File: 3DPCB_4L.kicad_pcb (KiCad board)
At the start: 4 copper layers, 100 x 60 mm, 740 parts, among them IC1 A5984_LP, IC2 A5984_LP, IC3 A5984_LP, IC4 A5984_LP, IC5 A5984_LP, IC6 MP9943, J10 , J11 , J12 , J13 , J14 , J15 , J16 , J2 , J3 , J4 , J5 , J6 , J7 , J8 , J9 , K1 CONN_3, K2 CONN_3, K3 CONN_3, K4 CONN_3, K5 CONN_3, K6 CONN_3, K7 CONN_3, K8 CONN_3, K9 CONN_3, P1 CONN_8, P11 CONN_3X2, P12 CONN_3X2, P13 CONN_4, P2 CONN_8, P5 CONN_4, P6 CONN_4, P7 CONN_4, P8 CONN_02X03, P9 CONN_4, U1 CONN_4_LERCHE, U10 MICRO-SD, U11 TC4427, U12 MCP4728, U13 CONN_4_LERCHE, U15 SPST_MOMENTARY, U16 CONN_4_LERCHE, U2 SPST_MOMENTARY, U21 CONN_4_LERCHE, U22 CONN_4_LERCHE, U23 MCP4728, U24 IRFH5302, U25 CONN_4_LERCHE, U3 BSS84, U4 CONN_4_LERCHE, U5 IRFH5302, U6 LPC1768_TQFP100, U7 IRFH5302, U8 IRFH5302, U9 TC4427

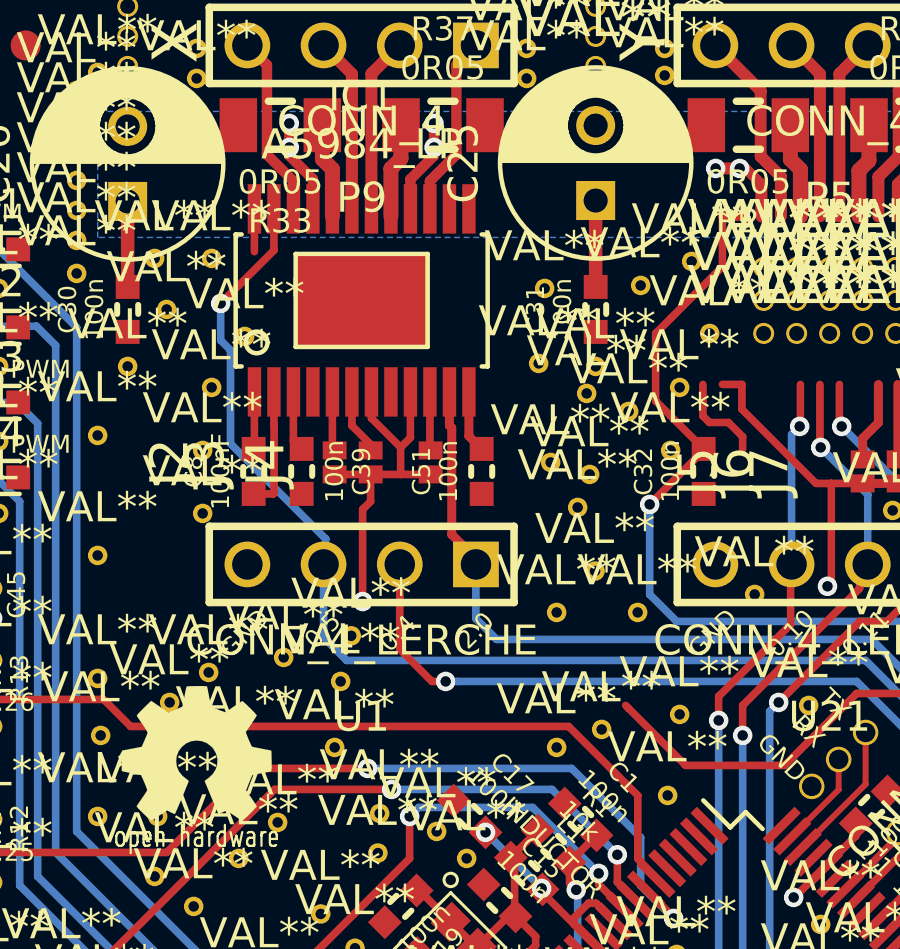
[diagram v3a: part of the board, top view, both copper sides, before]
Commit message: DONT USE NOW
Still working on PCB.
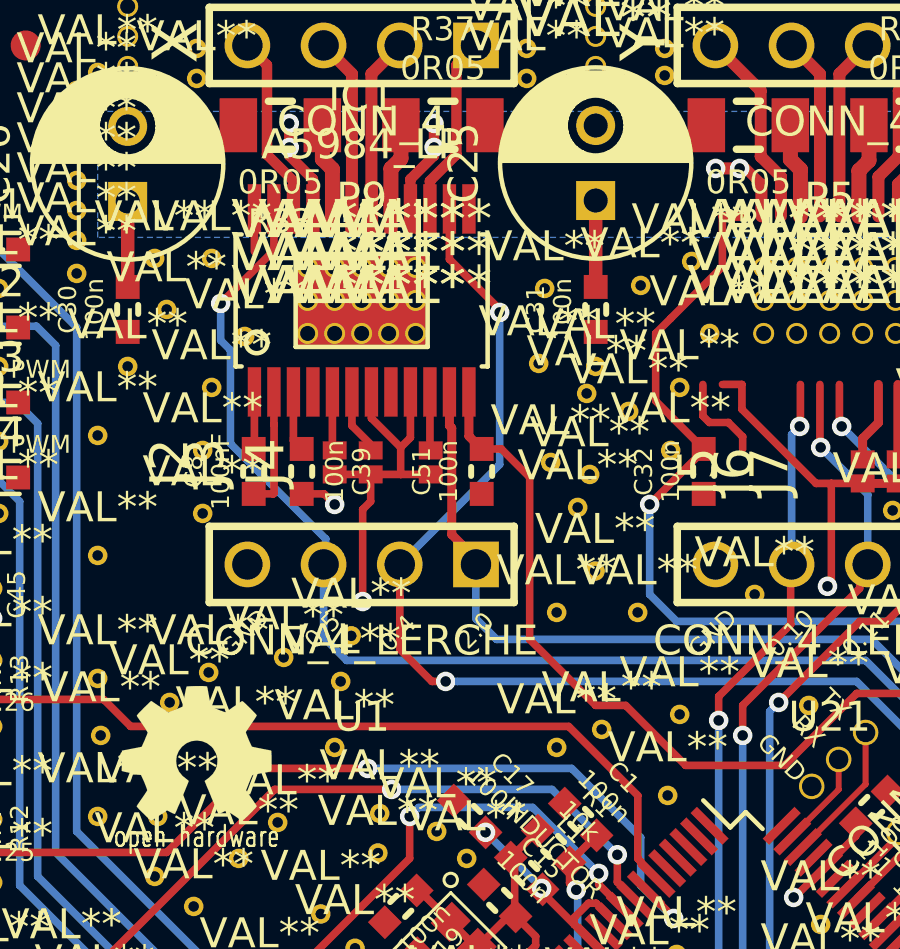
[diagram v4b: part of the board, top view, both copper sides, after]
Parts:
- added ?: VAL**, Lerche_via_0.5mm_GND, F.Cu at (150.6, 147.4)
- added ?: VAL**, Lerche_via_0.5mm_GND, F.Cu at (151.5, 145.2)
- added ?: VAL**, Lerche_via_0.5mm_GND, F.Cu at (149.7, 145.2)
- added ?: VAL**, Lerche_via_0.5mm_GND, F.Cu at (147.9, 145.2)
- added ?: VAL**, Lerche_via_0.5mm_GND, F.Cu at (147.9, 146.3)
- added ?: VAL**, Lerche_via_0.5mm_GND, F.Cu at (151.5, 146.3)
- added ?: VAL**, Lerche_via_0.5mm_GND, F.Cu at (149.7, 146.3)
- added ?: VAL**, Lerche_via_0.5mm_GND, F.Cu at (150.6, 146.3)
- added ?: VAL**, Lerche_via_0.5mm_GND, F.Cu at (150.6, 145.2)
- added ?: VAL**, Lerche_via_0.5mm_GND, F.Cu at (148.8, 145.2)
- added ?: VAL**, Lerche_via_0.5mm_GND, F.Cu at (148.8, 146.3)
- added ?: VAL**, Lerche_via_0.5mm_GND, F.Cu at (148.8, 147.4)
- added ?: VAL**, Lerche_via_0.5mm_GND, F.Cu at (147.9, 147.4)
- added ?: VAL**, Lerche_via_0.5mm_GND, F.Cu at (149.7, 147.4)
- added ?: VAL**, Lerche_via_0.5mm_GND, F.Cu at (151.5, 147.4)
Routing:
- net DIR1: track 33.0 -> 46.9 mm, vias 2 -> 3
- net VREF1: track 31.9 -> 43.4 mm
- net +12V: track 55.1 -> 56.3 mm, vias 9 -> 10

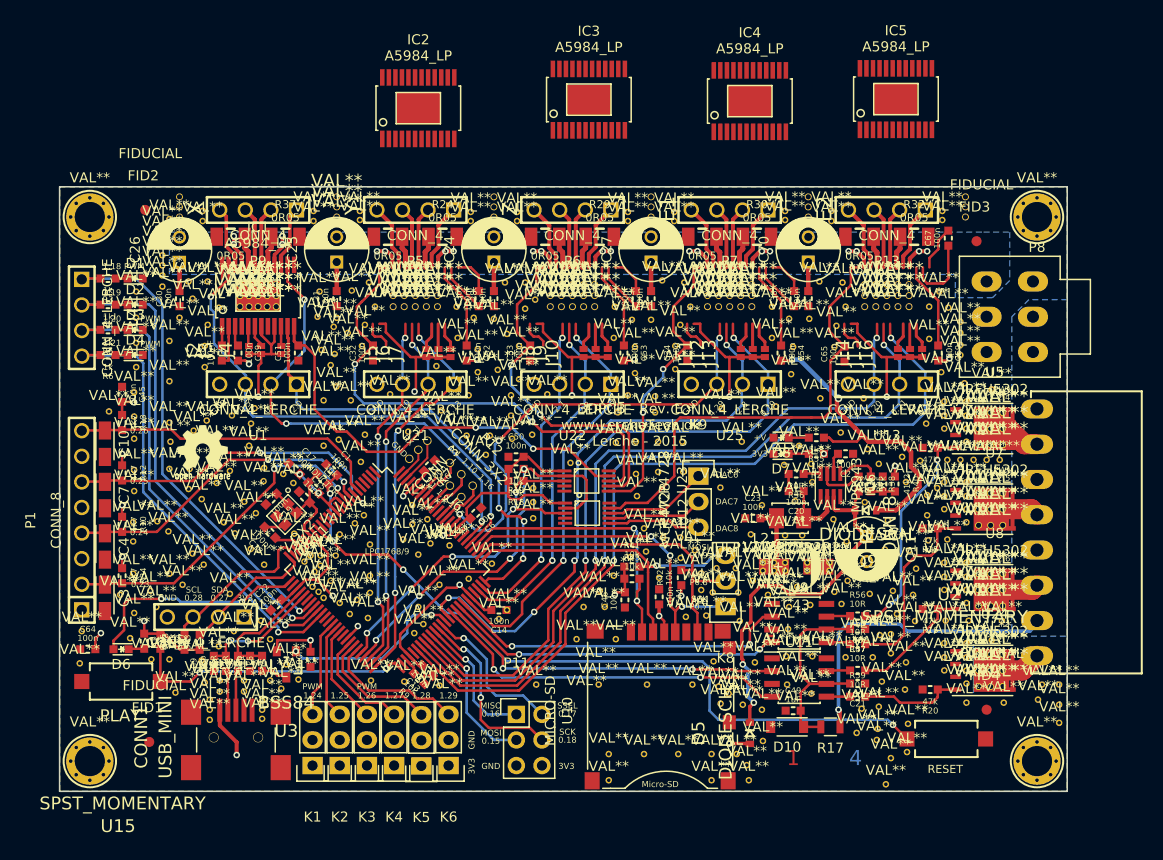
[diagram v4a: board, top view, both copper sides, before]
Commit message: Wired all connections with A5984 on PCB
UNTESTED - Do not use now.
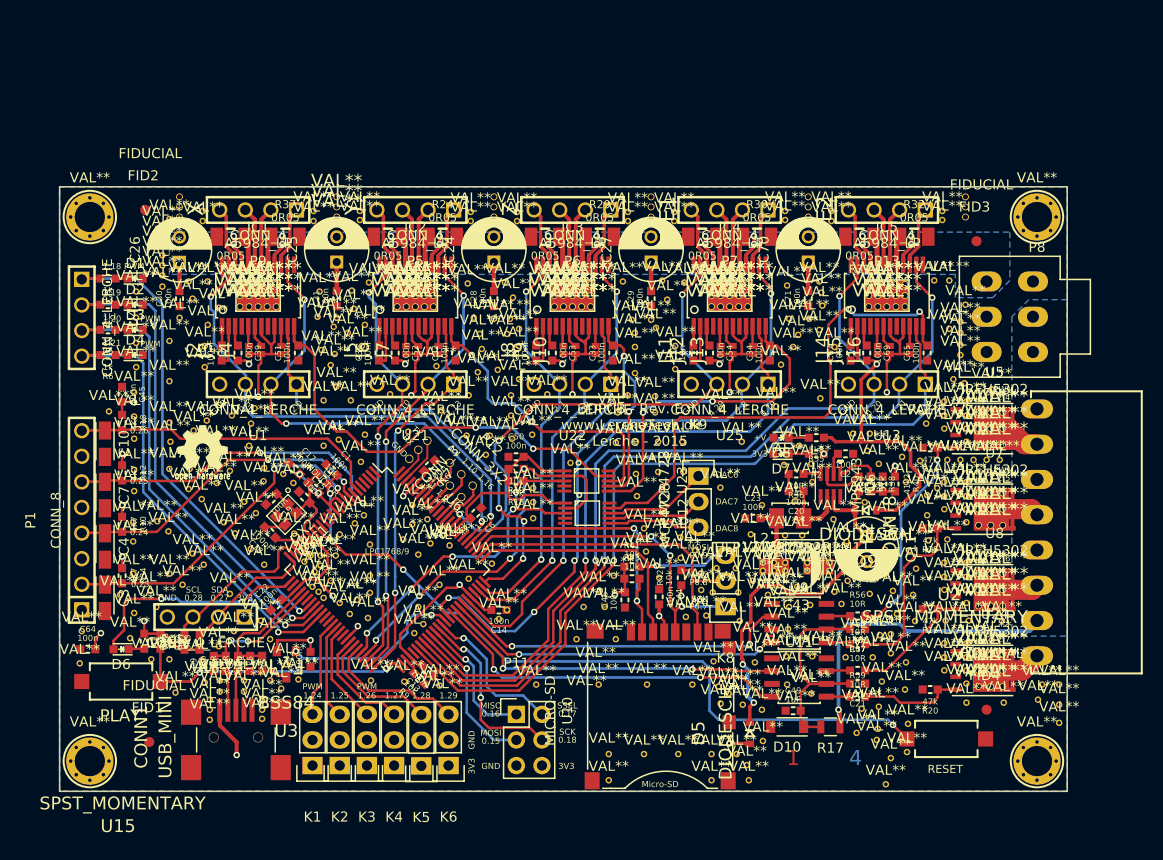
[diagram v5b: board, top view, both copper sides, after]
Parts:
- moved IC5 19.5 mm to (212.1, 146.3)
- moved IC3 19.5 mm to (180.9, 146.3)
- moved IC4 19.4 mm to (196.5, 146.3)
- moved IC2 18.6 mm to (165.3, 146.3)
- moved C67 15.0 mm to (208.5, 152.0)
- moved C38 11.4 mm to (192.9, 152.0)
- moved C36 11.3 mm to (161.7, 152.0)
- moved C37 11.3 mm to (177.3, 152.0)
- moved ? 9.14 mm to (218.3, 144.8)
- moved C65 8.20 mm to (216.1, 152.0)
- moved C32 8.20 mm to (169.3, 152.0)
- moved C33 8.20 mm to (184.9, 152.0)
- moved C34 8.20 mm to (200.5, 152.0)
- moved ? 7.59 mm to (218.7, 154.6)
- moved C52 7.10 mm to (163.3, 152.0)
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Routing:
- net (no net): track 35.6 -> 0.68 mm, vias 16 -> 0
- net +12V: track 56.3 -> 78.6 mm, vias 10 -> 25
- net VREF2: track 49.8 -> 29.9 mm
- net VREF3: track 35.1 -> 19.3 mm
- net EN5: track 73.4 -> 81.2 mm
- net EN4: track 45.4 -> 53.3 mm
- net EN3: track 32.5 -> 40.4 mm
- net EN2: track 35.4 -> 43.2 mm
- net DIR2: track 38.0 -> 45.4 mm
- net DIR5: track 77.0 -> 84.2 mm
- net DIR3: track 35.0 -> 42.1 mm
- net DIR4: track 57.8 -> 64.7 mm
- net Net-(C53-Pad2): track 8.65 -> 2.01 mm
- net Net-(C52-Pad2): track 8.65 -> 2.01 mm
- net Net-(C69-Pad2): track 8.65 -> 2.01 mm
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
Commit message: Moved vias around
Moved vias around
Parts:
- added ?: VAL**, Lerche_via_0.35mm_GND_MaskOver, F.Cu at (228.7, 145.4)
- added ?: VAL**, Lerche_via_0.35mm_GND_MaskOver, F.Cu at (220.6, 150.2)
- added ?: VAL**, Lerche_via_0.35mm_GND_MaskOver, F.Cu at (189.6, 166.7)
- added ?: VAL**, Lerche_via_0.35mm_GND_MaskOver, F.Cu at (191.3, 167.4)
- added ?: VAL**, Lerche_via_0.35mm_GND_MaskOver, F.Cu at (201.1, 164.8)
- added ?: VAL**, Lerche_via_0.35mm_GND_MaskOver, F.Cu at (198.8, 157.6)
- added ?: VAL**, Lerche_via_0.35mm_GND_MaskOver, F.Cu at (193.9, 157.7)
- added ?: VAL**, Lerche_via_0.35mm_GND_MaskOver, F.Cu at (197.7, 159.1)
- added ?: VAL**, Lerche_via_0.35mm_GND_MaskOver, F.Cu at (203.3, 155.1)
- added ?: VAL**, Lerche_via_0.35mm_GND_MaskOver, F.Cu at (207.3, 156.8)
- added ?: VAL**, Lerche_via_0.35mm_GND_MaskOver, F.Cu at (201.3, 144.9)
- added ?: VAL**, Lerche_via_0.35mm_GND_MaskOver, F.Cu at (228.6, 143.0)
- added ?: VAL**, Lerche_via_0.35mm_GND_MaskOver, F.Cu at (201.6, 147.9)
- added ?: VAL**, Lerche_via_0.35mm_GND_MaskOver, F.Cu at (184.5, 147.7)
- added ?: VAL**, Lerche_via_0.35_GND_MaskOver, F.Cu at (173.0, 148.5)
- added ?: VAL**, Lerche_via_0.35mm_GND_MaskOver, F.Cu at (226.9, 143.0)
- added ?: VAL**, Lerche_via_0.35mm_GND_MaskOver, F.Cu at (225.3, 143.0)
- added ?: VAL**, Lerche_via_0.35mm_GND_MaskOver, F.Cu at (224.9, 145.9)
- added ?: VAL**, Lerche_via_0.35mm_GND_MaskOver, F.Cu at (223.7, 147.1)
- added ?: VAL**, Lerche_via_0.35mm_GND_MaskOver, F.Cu at (223.7, 150.2)
- added ?: VAL**, Lerche_via_0.35mm_GND_MaskOver, F.Cu at (223.7, 153.3)
- added ?: VAL**, Lerche_via_0.35mm_GND_MaskOver, F.Cu at (220.6, 153.3)
- moved ? 8.86 mm to (217.7, 145.8)
- moved ? 6.99 mm to (153.0, 147.4)
- moved ? 5.02 mm to (175.7, 152.9)
- moved ? 4.44 mm to (172.2, 157.4)
- moved ? 3.89 mm to (160.6, 153.0)
- moved ? 3.72 mm to (155.1, 148.8)
- moved ? 3.56 mm to (177.3, 146.5)
- moved ? 3.29 mm to (201.7, 154.5)
- moved ? 3.22 mm to (155.8, 146.5)
- moved ? 3.11 mm to (205.6, 152.8)
- moved ? 3.00 mm to (161.8, 146.2)
- moved ? 2.92 mm to (199.7, 147.5)
- moved ? 2.80 mm to (156.2, 154.5)
- moved ? 2.55 mm to (217.4, 147.2)
- moved ? 2.40 mm to (155.1, 150.8)
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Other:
- board text added: "3DPCB www.LercheTech.dk C. Lerche - 2016"
- board text removed: "3DPCB - Rev. E www.LercheTech.dk C. Lerche - 2015"

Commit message: Still doing work
Still doing work
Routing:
- removed copper zone on B.Cu, net /P2.7_FET
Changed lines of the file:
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@@
-(kicad_pcb (version 4) (host pcbnew 4.0.2-stable)
+(kicad_pcb (version 4) (host pcbnew 4.0.4-stable)
   (general
     (links 1072)
     (no_connects 0)
-    (area 125.893917 130.7236 237.651491 200.3226)
+    (area 129.924999 135.424999 230.075001 195.575001)
     (thickness 1.6)
     (drawings 131)
@@
   (layers
     (0 F.Cu mixed)
-    (1 Inner2.Cu power hide)
-    (2 Inner1.Cu power hide)
+    (1 Inner2.Cu power)
+    (2 Inner1.Cu power)
     (31 B.Cu mixed)
     (32 B.Adhes user)
@@
     (trace_clearance 0.1524)
     (zone_clearance 0.16)
-    (zone_45_only no)
+    (zone_45_only yes)
     (trace_min 0.1524)
     (segment_width 0.2)
@@
     (polygon
       (pts
-        (xy 230 195.5) (xy 130 195.5) (xy 130 135.5) (xy 230 135.5) (xy 230 195.5)
+        (xy 230 195.5) (xy 130 195.5) (xy 130 135.5) (xy 230 135.5)
       )
     )
@@
     (polygon
       (pts
-        (xy 224.3 143.9) (xy 224.3 144.8) (xy 224.3 144.8) (xy 222.6 146.5) (xy 218.9 146.5)
-        (xy 218.9 144.2) (xy 140.9 144.2) (xy 140.9 140) (xy 221.7 140) (xy 224.3 140)
-        (xy 224.3 142.8) (xy 224.3 142.8)
-      )
-    )
-  )
-  (zone (net 4) (net_name /P2.7_FET) (layer B.Cu) (hatch edge 0.508)
-    (priority 1)
-    (connect_pads yes (clearance 0.2))
-    (min_thickness 0.2)
-    (fill yes (arc_segments 16) (thermal_gap 0.25) (thermal_bridge_width 0.25))
-    (polygon
-      (pts
-        (xy 220.7 185.7) (xy 220.7 180.9) (xy 220.7 185.7)
+        (xy 224.3 143.9) (xy 224.3 144.8) (xy 222.6 146.5) (xy 218.9 146.5) (xy 218.9 144.2)
+        (xy 140.9 144.2) (xy 140.9 140) (xy 221.7 140) (xy 224.3 140) (xy 224.3 142.8)
+        (xy 224.3 142.8)
       )
     )
@@
     (polygon
       (pts
-        (xy 230 141.5) (xy 224 141.5) (xy 224 135.5) (xy 230 135.5)
+        (xy 230 142) (xy 223.5 142) (xy 223.5 135.5) (xy 230 135.5)
       )
     )
@@
     (polygon
       (pts
-        (xy 230 146.7) (xy 226.2 146.7) (xy 226.2 146.7) (xy 224.5 148.4) (xy 224.5 180.1)
-        (xy 230 180.1)
+        (xy 230 146.7) (xy 226.2 146.7) (xy 224.5 148.4) (xy 224.5 180.1) (xy 230 180.1)
       )
     )
@@
       )
     )
+  )
+  (zone (net 0) (net_name "") (layer B.Cu) (hatch edge 0.508)
+    (connect_pads (clearance 0.16))
+    (min_thickness 0.254)
+    (keepout (tracks allowed) (vias allowed) (copperpour not_allowed))
+    (fill (arc_segments 16) (thermal_gap 0.508) (thermal_bridge_width 0.508))
+    (polygon
+      (pts
+        (xy 223.5 135.5) (xy 230 135.5) (xy 230 142) (xy 223.5 142)
+      )
+    )
+  )
+  (zone (net 0) (net_name "") (layer Inner2.Cu) (hatch edge 0.508)
+    (connect_pads (clearance 0.16))
+    (min_thickness 0.254)
+    (keepout (tracks allowed) (vias allowed) (copperpour not_allowed))
+    (fill (arc_segments 16) (thermal_gap 0.508) (thermal_bridge_width 0.508))
+    (polygon
+      (pts
+        (xy 223.506027 135.5) (xy 230.006027 135.5) (xy 230.006027 142) (xy 223.506027 142)
+      )
+    )
+  )
+  (zone (net 0) (net_name "") (layer Inner1.Cu) (hatch edge 0.508)
+    (connect_pads (clearance 0.16))
+    (min_thickness 0.254)
+    (keepout (tracks allowed) (vias allowed) (copperpour not_allowed))
+    (fill (arc_segments 16) (thermal_gap 0.508) (thermal_bridge_width 0.508))
+    (polygon
+      (pts
+        (xy 223.5 135.5) (xy 230 135.5) (xy 230 142) (xy 223.5 142)
+      )
+    )
